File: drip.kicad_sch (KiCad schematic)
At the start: 79 parts, among them J1 ISP, Q1 2n2907, Q2 2n2907, Q3 2n2907, Q4 2n2907, Q5 2n2907, Q6 2n2907, Q7 2n2907, Q8 2n2907, U1 74LS138, U2 5641AS-4Digit-7Segment, U3 5641AS-4Digit-7Segment, U4 MSP430G2553IN20

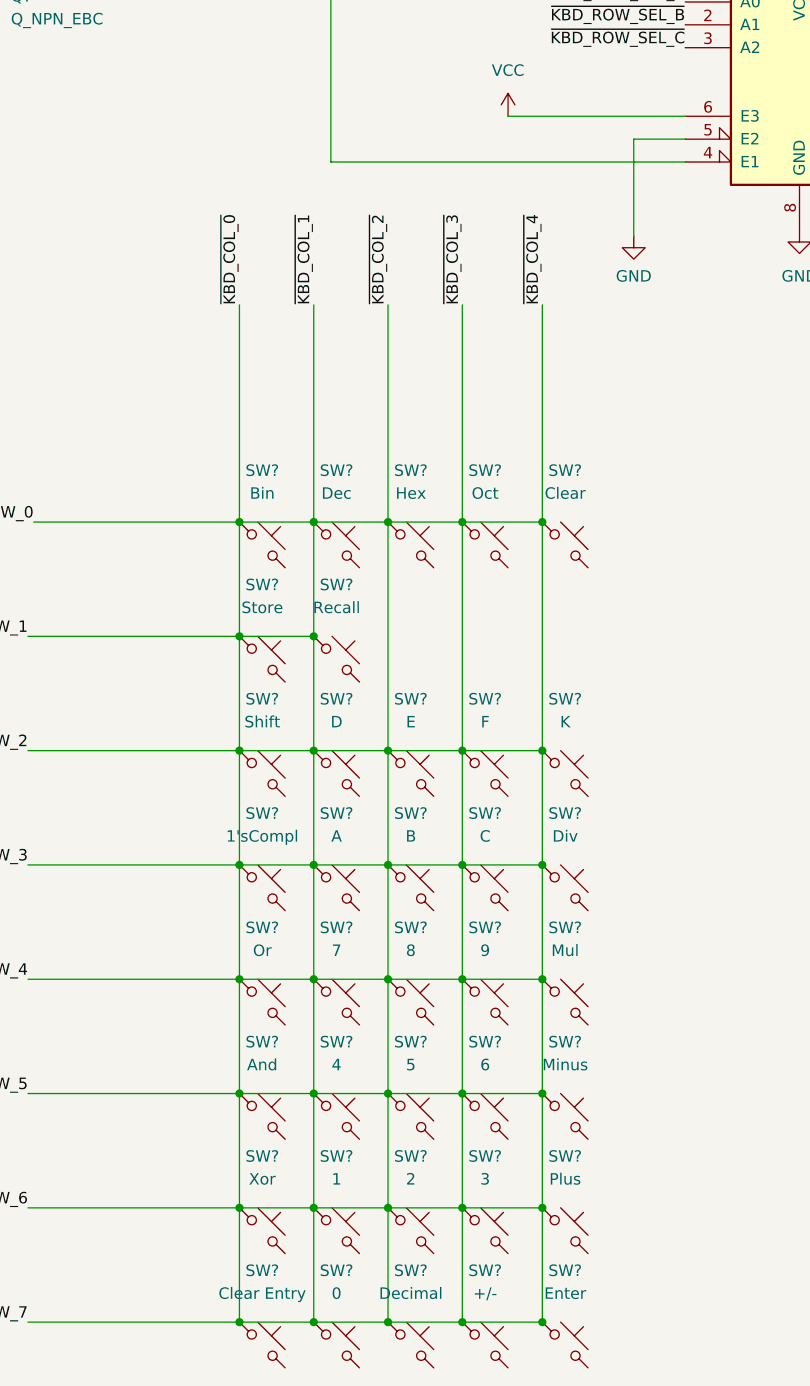
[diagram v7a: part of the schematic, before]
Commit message: Wire the keyboard matrix properly this time
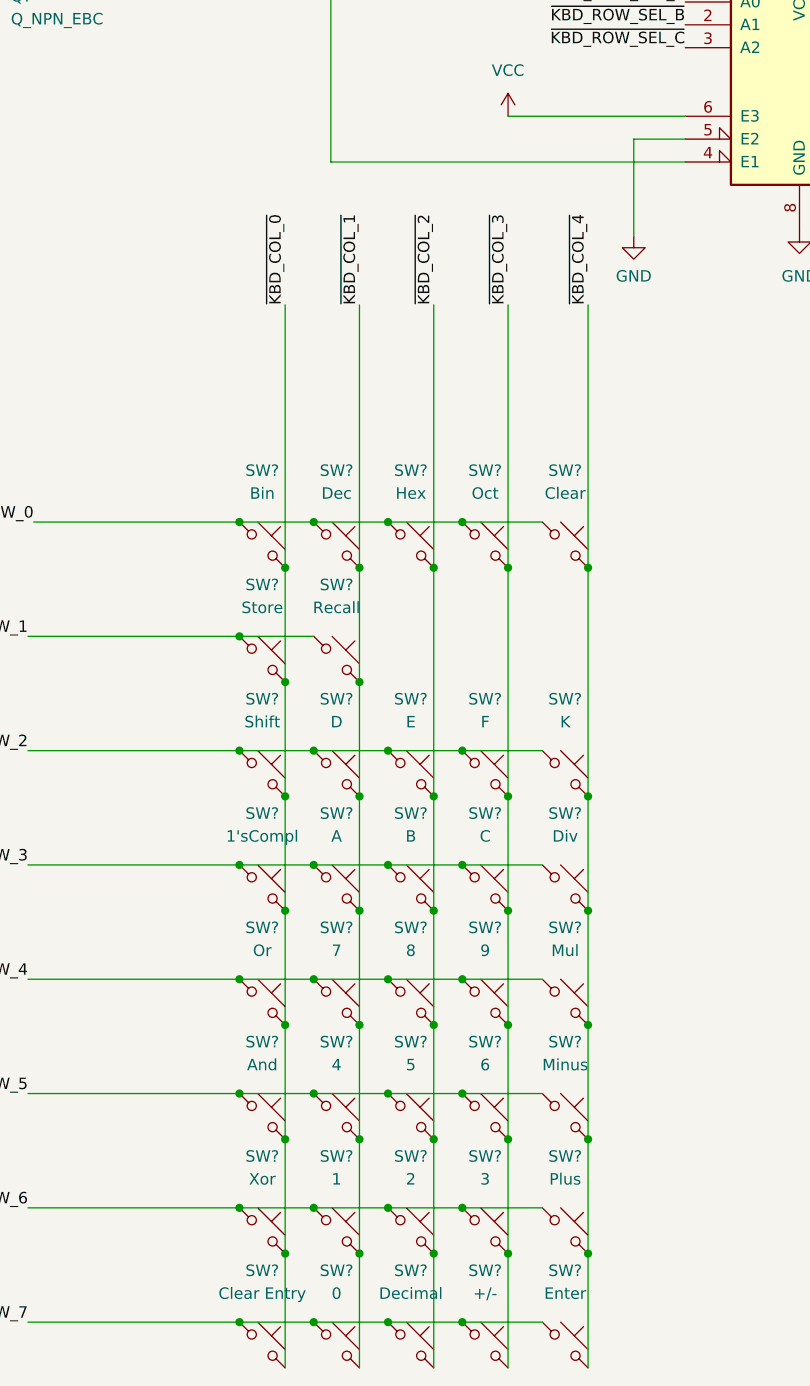
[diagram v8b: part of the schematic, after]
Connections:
- net KBD_ROW_0: no longer SW?.1, SW?.1, SW?.1, SW?.1, SW?.1, SW?.1, SW?.1, SW?.1, SW?.1, SW?.1, SW?.1, SW?.1, SW?.1, SW?.1, SW?.1, SW?.1, SW?.1, SW?.1, SW?.1, SW?.1, SW?.1, SW?.1, SW?.1, SW?.1, SW?.1, SW?.1, SW?.1, SW?.1, SW?.1, SW?.1, SW?.1, SW?.1, U?.1 (I3), U?.11 (O4), U?.12 (I7), U?.12 (O3), U?.13 (I6), U?.13 (O2), U?.14 (I5), U?.14 (O1), U?.15 (I4), U?.15 (O0), U?.2 (I2), U?.3 (I1)
- net ~{KBD_COL_0}: now reaches SW?.2
- net ~{KBD_COL_0}: now also SW?.2, SW?.2, SW?.2, SW?.2, SW?.2, SW?.2, SW?.2, U?.15 (O0)
- net ~{KBD_COL_2}: now reaches SW?.2
- net ~{KBD_COL_2}: now also SW?.2, SW?.2, SW?.2, SW?.2, SW?.2, SW?.2, U?.13 (O2)
- net ~{KBD_COL_3}: now reaches SW?.2
- net ~{KBD_COL_3}: now also SW?.2, SW?.2, SW?.2, SW?.2, SW?.2, SW?.2, U?.12 (O3)
- net ~{KBD_COL_4}: now reaches SW?.2
- net ~{KBD_COL_4}: now also SW?.2, SW?.2, SW?.2, SW?.2, SW?.2, SW?.2, U?.11 (O4)
- net ~{KBD_COL_1}: now reaches SW?.2
- net ~{KBD_COL_1}: now also SW?.2, SW?.2, SW?.2, SW?.2, SW?.2, SW?.2, SW?.2, U?.14 (O1)
- new net KBD_ROW_1: SW?.1, SW?.1, U?.3 (I1)
- new net KBD_ROW_2: SW?.1, SW?.1, SW?.1, SW?.1, SW?.1, U?.2 (I2)
- new net KBD_ROW_3: SW?.1, SW?.1, SW?.1, SW?.1, SW?.1, U?.1 (I3)
- new net KBD_ROW_4: SW?.1, SW?.1, SW?.1, SW?.1, SW?.1, U?.15 (I4)
- new net KBD_ROW_5: SW?.1, SW?.1, SW?.1, SW?.1, SW?.1, U?.14 (I5)
- new net KBD_ROW_6: SW?.1, SW?.1, SW?.1, SW?.1, SW?.1, U?.13 (I6)
- new net KBD_ROW_7: SW?.1, SW?.1, SW?.1, SW?.1, SW?.1, U?.12 (I7)
